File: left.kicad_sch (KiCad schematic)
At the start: 121 parts, among them J1 Pointing stick, J4 Conn_01x03_Male, J6 Conn_01x01_Female, SW1 SW_Push, SW16 SW_Push, SW17 SW_Push, SW18 SW_Push, SW19 SW_Push, SW2 SW_Push, SW20 SW_Push, SW21 SW_Push, SW22 SW_Push, SW3 SW_Push, SW31 SW_Push, SW32 SW_Push, SW33 SW_Push, SW34 SW_Push, SW35 SW_Push, SW36 SW_Push, SW37 SW_Push, SW4 SW_Push, SW46 SW_Push, SW47 SW_Push, SW48 SW_Push, SW49 SW_Push, SW5 SW_Push, SW50 SW_Push, SW51 SW_Push, SW6 SW_Push, SW61 SW_Push, SW62 SW_Push, SW63 SW_Push, SW64 SW_Push, SW65 SW_Push, SW66 SW_Push, SW7 SW_Push, SW76 SW_Push, SW77 SW_Push, SW78 SW_Push, SW79 SW_Push, SW80 SW_Push, SW81 SW_Push, SW82 SW_Push, U1 Elite-C

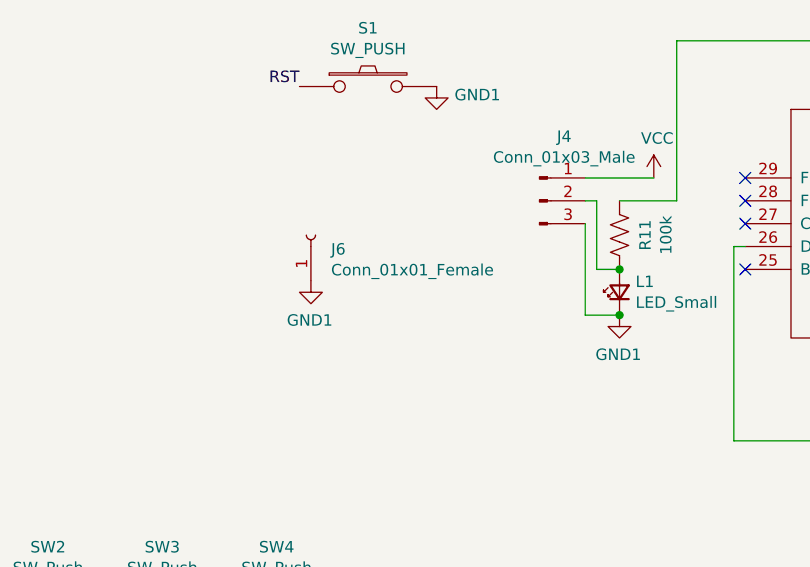
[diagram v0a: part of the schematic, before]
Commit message: make changes for higher mcu position/potential bat
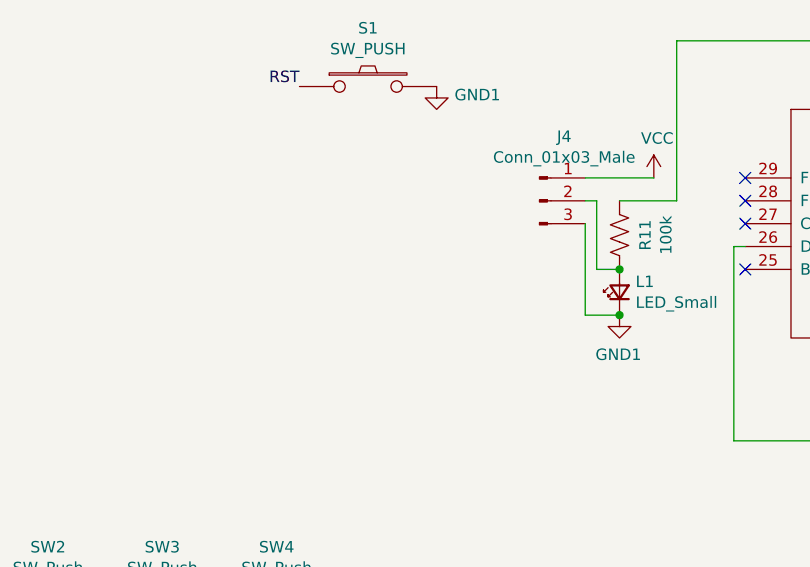
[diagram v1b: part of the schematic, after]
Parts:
- removed J6: Conn_01x01_Female, TestPoint:TestPoint_Pad_1.0x1.0mm, symbol Connector:Conn_01x01_Female
